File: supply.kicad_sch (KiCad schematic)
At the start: 6 parts

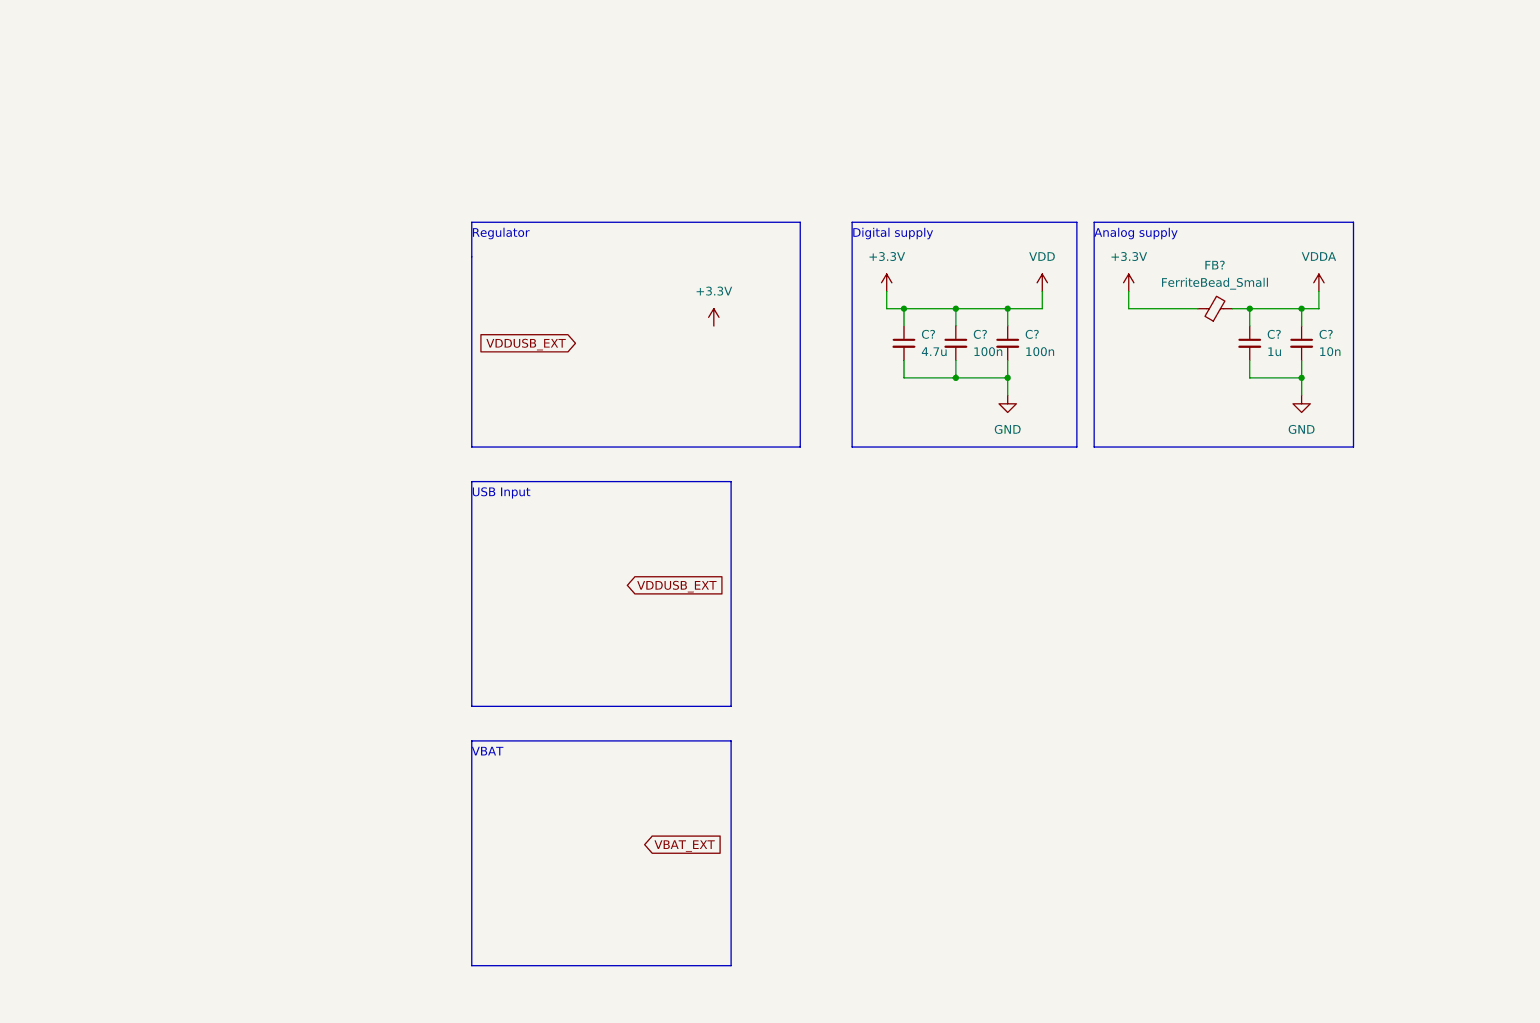
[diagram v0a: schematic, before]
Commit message: Supply: - Added voltage regulator - appended calculations for L and Voltage divider - Added USB-C connector symbol and connected D+/D- lines
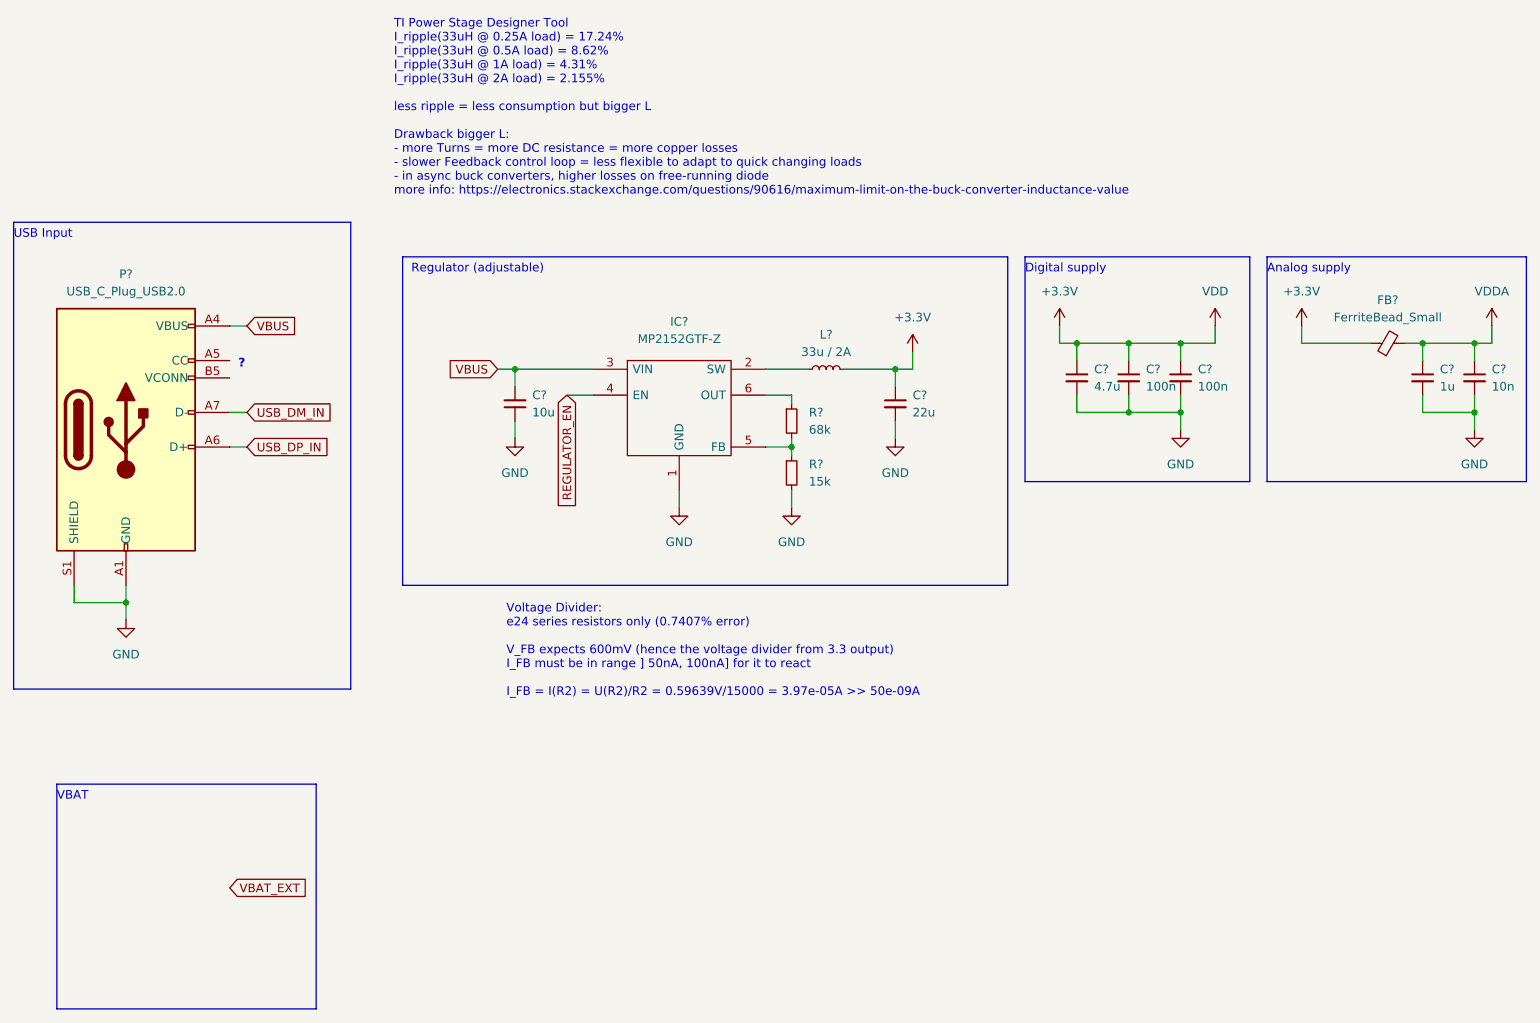
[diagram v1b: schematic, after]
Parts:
- added C?: 10u, Capacitor_SMD:C_0603_1608Metric, symbol Device:C_Small
- added C?: 22u, Capacitor_SMD:C_0603_1608Metric, symbol Device:C_Small
- added IC?: MP2152GTF-Z, CustomKeyboard:MP2152GTF33P, symbol CustomKeyboard:MP2152GTF-Z
- added L?: 33u / 2A, symbol Device:L_Small
- added P?: USB_C_Plug_USB2.0, symbol Connector:USB_C_Plug_USB2.0
- added R?: 68k, Resistor_SMD:R_0603_1608Metric, symbol Device:R_Small
- added R?: 15k, symbol Device:R_Small
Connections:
- net +3.3V: now also C?.1, L?.2
- net GND: now also C?.1, C?.2, IC?.1 (GND), P?.A1 (GND), P?.A12 (GND), P?.B1 (GND), P?.B12 (GND), P?.S1 (SHIELD), R?.2
- new net: IC?.6 (OUT), R?.1
- new net: IC?.5 (FB), R?.1, R?.2
- new net: IC?.2 (SW), L?.1
- new net REGULATOR_EN: IC?.4 (EN)
- new net USB_DM_IN: P?.A7 (D-)
- new net USB_DP_IN: P?.A6 (D+)
- new net VBUS: C?.2, IC?.3 (VIN), P?.A4 (VBUS), P?.A9 (VBUS), P?.B4 (VBUS), P?.B9 (VBUS)
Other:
- note added: "?"
- note added: "Regulator (adjustable)"
- note added: "TI Power Stage Designer Tool I_ripple(33uH @ 0.25A load) = 17.24% I_ripple(33uH @ 0.5A load) = 8.62% I_ripple(33uH @ 1A load) = 4.31% I_ripple(33uH @ 2A load) = 2.155% less ripple = less consumption but bigger L Drawback bigger L: - more Turns = more DC resistance = more copper losses - slower Feedback control loop = less flexible to adapt to quick changing loads - in async buck converters, highe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"
- note added: "Voltage Divider: e24 series resistors only (0.7407% error) V_FB expects 600mV (hence the voltage divider from 3.3 output) I_FB must be in range ] 50nA, 100nA] for it to react I_FB = I(R2) = U(R2)/R2 = 0.59639V/15000 = 3.97e-05A >> 50e-09A"
- note removed: "Regulator"
- moved on the sheet: C?, FB?

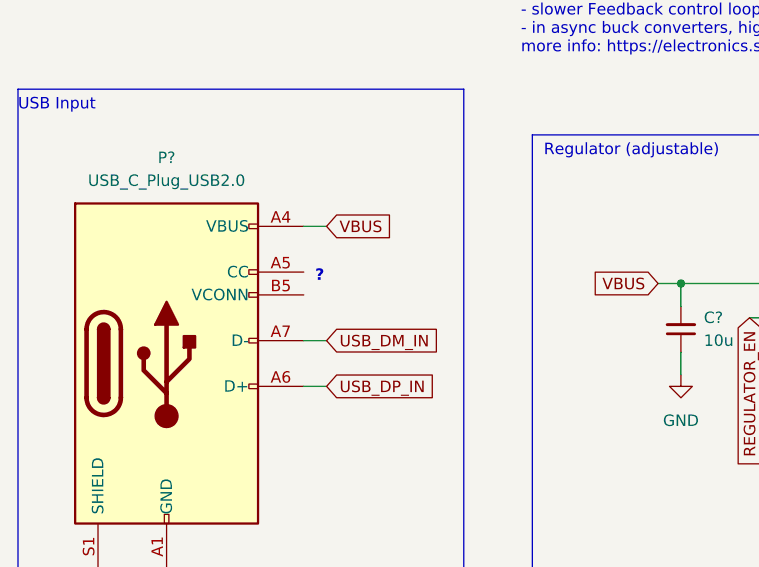
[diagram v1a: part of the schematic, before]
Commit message: Added CC1 / CC2
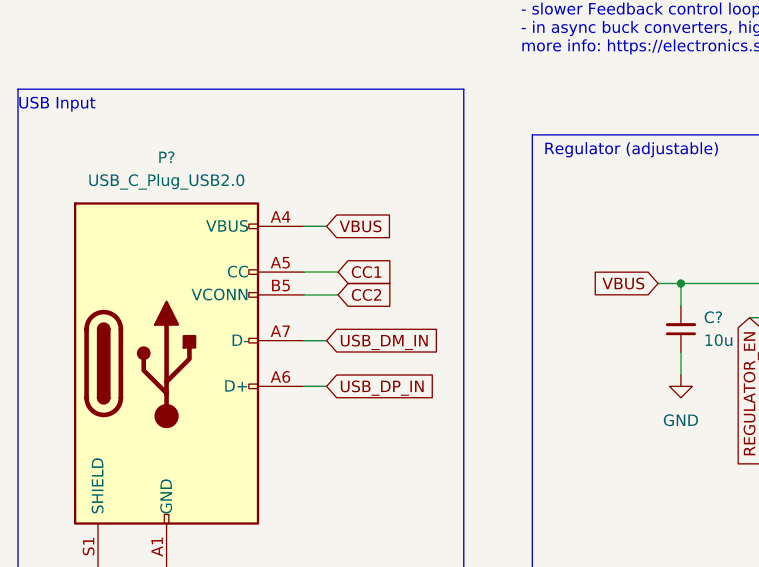
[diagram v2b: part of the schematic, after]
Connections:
- net CC1: now reaches P?.A5 (CC)
- net CC2: now reaches P?.B5 (VCONN)
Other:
- note removed: "?"
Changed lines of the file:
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@@
+    (stroke (width 0) (type default) (color 0 0 0 0))
+  )
+  (wire (pts (xy 50.8 93.98) (xy 54.61 93.98))
     (stroke (width 0) (type default) (color 0 0 0 0))
   )
@@
   )
   (polyline (pts (xy 68.58 71.12) (xy 19.05 71.12))
+    (stroke (width 0) (type default) (color 0 0 0 0))
+  )
+  (wire (pts (xy 50.8 91.44) (xy 54.61 91.44))
     (stroke (width 0) (type default) (color 0 0 0 0))
   )
@@
     (effects (font (size 1.27 1.27)) (justify left bottom))
   )
-  (text "?" (at 52.07 92.71 0)
-    (effects (font (size 1.27 1.27) (thickness 0.254) bold) (justify left bottom))
-  )
   (text "VBAT" (at 25.4 156.21 0)
     (effects (font (size 1.27 1.27)) (justify left bottom))
@@
       (effects (font (size 1.27 1.27)) (justify left) hide)
     )
+  )
+  (global_label "CC2" (shape input) (at 54.61 93.98 0) (fields_autoplaced)
+    (effects (font (size 1.27 1.27)) (justify left))
+    (property "Intersheet References" "${INTERSHEET_REFS}" (id 0) (at 60.6837 93.9006 0)
+      (effects (font (size 1.27 1.27)) (justify left) hide)
+    )
+  )
+  (global_label "CC1" (shape input) (at 54.61 91.44 0) (fields_autoplaced)
+    (effects (font (size 1.27 1.27)) (justify left))
+    (property "Intersheet References" "${INTERSHEET_REFS}" (id 0) (at 60.6837 91.3606 0)
+      (effects (font (size 1.27 1.27)) (justify left) hide)
+    )
